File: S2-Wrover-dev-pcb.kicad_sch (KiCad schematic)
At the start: 8 parts, among them P1 CONN_02X13

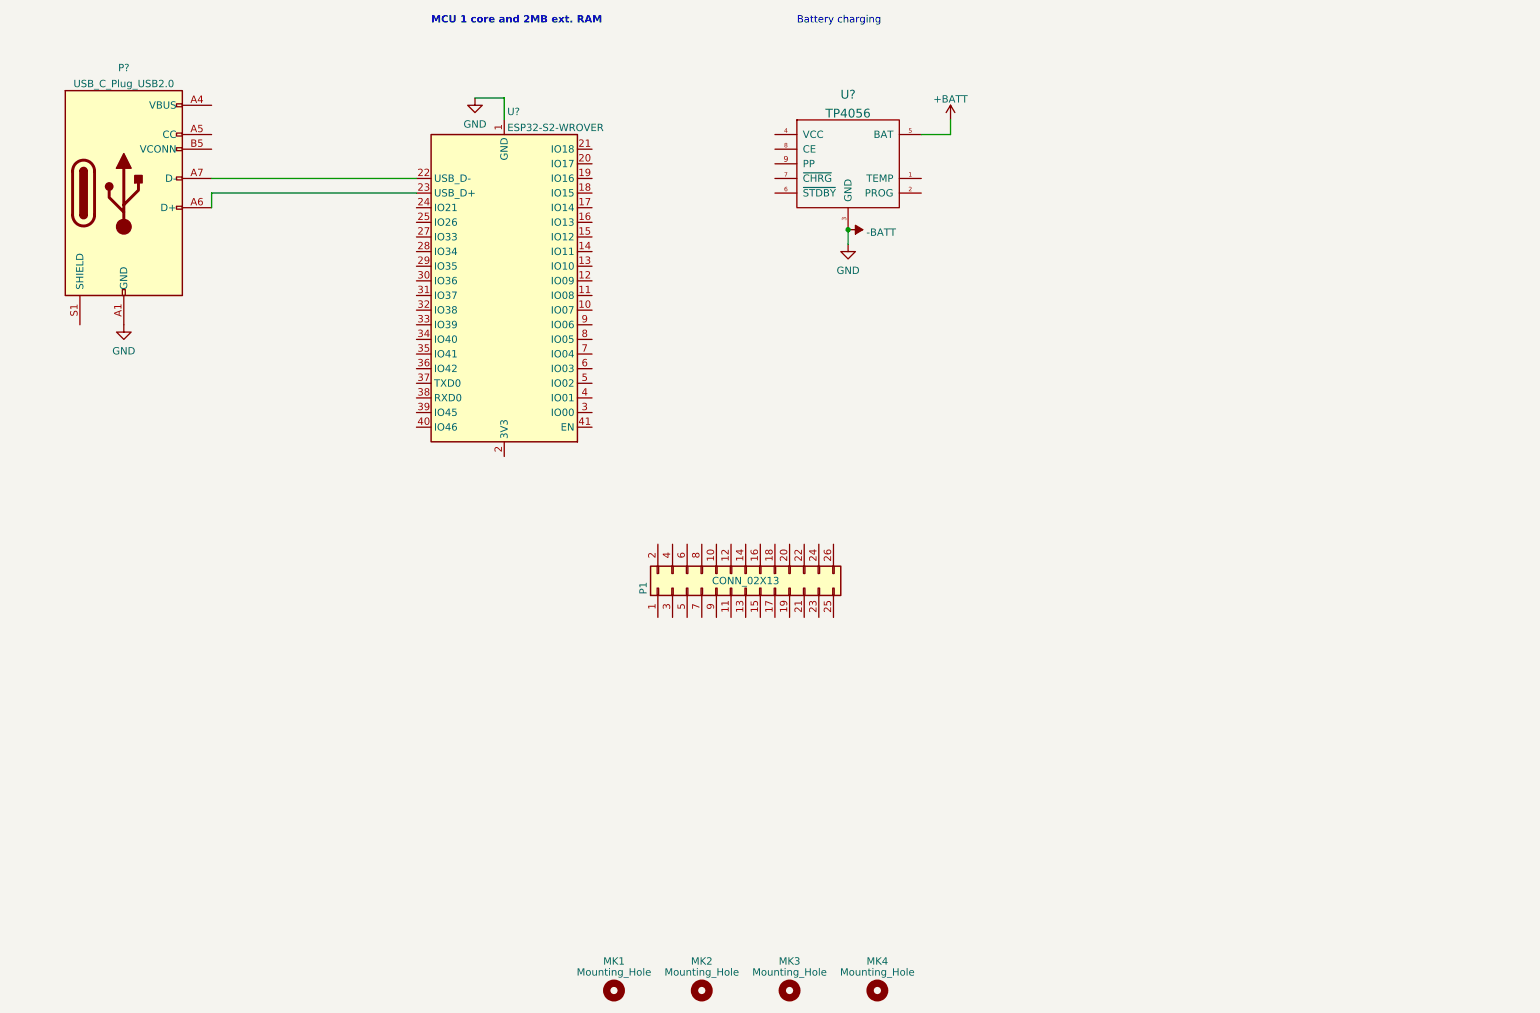
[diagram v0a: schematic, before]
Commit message: Add schematic
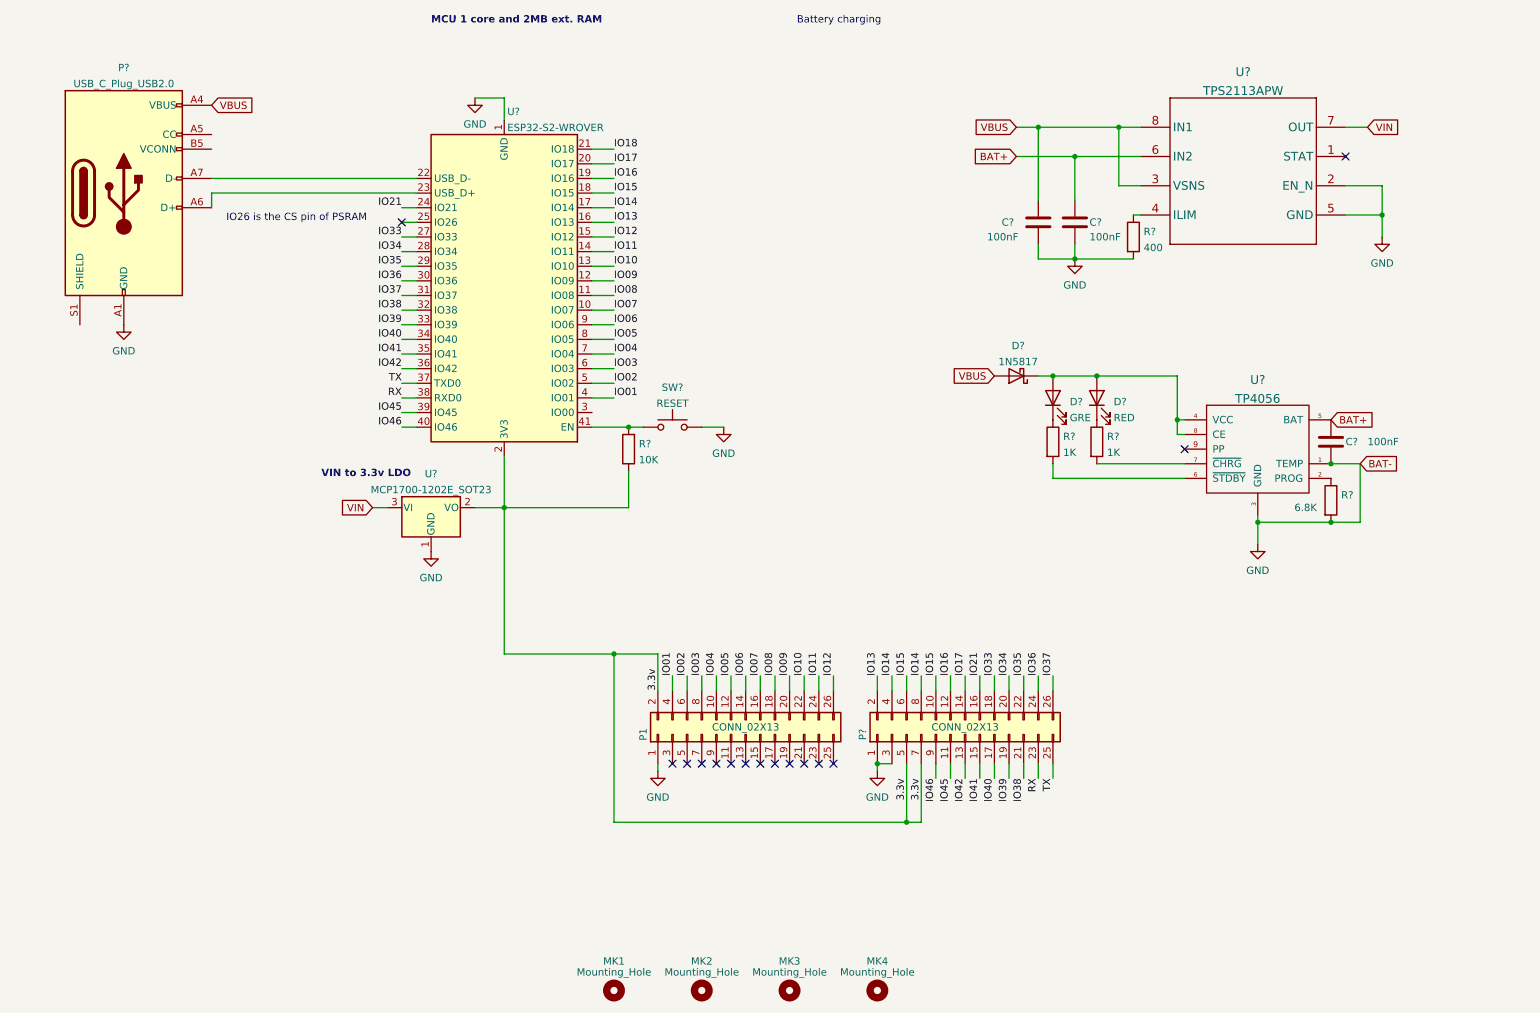
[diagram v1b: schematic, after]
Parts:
- added C? (x3): 100nF, Capacitor_SMD:C_0805_2012Metric, symbol Device:C
- added D?: 1N5817, Diode_SMD:D_SOD-123, symbol Device:D_Schottky
- added D?: RED, LED_SMD:LED_0805_2012Metric, symbol Device:LED
- added D?: GRE, LED_SMD:LED_0805_2012Metric, symbol Device:LED
- added P?: CONN_02X13, Pin_Headers:Pin_Header_Straight_2x13, symbol Connector_Generic:Conn_02x13_Odd_Even
- added R?: 400, Resistor_SMD:R_0603_1608Metric, symbol Device:R
- added R?: 6.8K, Resistor_SMD:R_0603_1608Metric, symbol Device:R
- added R? (x2): 1K, Resistor_SMD:R_0603_1608Metric, symbol Device:R
- added R?: 10K, Resistor_SMD:R_0603_1608Metric, symbol Device:R
- added SW?: RESET, Button_Switch_SMD:SW_SPST_B3U-1000P-B, symbol Switch:SW_Push
- added U?: TPS2113APW, PW0008A_N, symbol epd_breakout:TPS2113APW
- added U?: MCP1700-1202E_SOT23, Package_TO_SOT_SMD:SOT-23, symbol Regulator_Linear:MCP1700-1202E_SOT23
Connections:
- net -BATT is gone; now on net GND: P?.A1 (GND), P?.A12 (GND), P?.B1 (GND), P?.B12 (GND), U?.1 (GND), U?.26 (GND), U?.3 (GND), U?.42 (GND), U?.43 (GND)
- net GND: now reaches P1.1 (Pin_1)
- net GND: now also U?.1 (TEMP), C?.1, C?.1, C?.1, P?.1 (Pin_1), P?.3 (Pin_3), R?.2, R?.2, SW?.2, U?.1 (GND), U?.2 (EN_N), U?.5 (GND)
- net IO04: now reaches P1.10 (Pin_10)
- net IO04: now also U?.7 (IO04)
- net IO05: now reaches P1.12 (Pin_12)
- net IO05: now also U?.8 (IO05)
- net IO06: now reaches P1.14 (Pin_14)
- net IO06: now also U?.9 (IO06)
- net IO07: now reaches P1.16 (Pin_16)
- net IO07: now also U?.10 (IO07)
- net IO08: now reaches P1.18 (Pin_18)
- net IO08: now also U?.11 (IO08)
- net 3.3v: now reaches P1.2 (Pin_2)
- net 3.3v: now also U?.2 (3V3), P?.5 (Pin_5), P?.7 (Pin_7), R?.1, U?.2 (VO)
- net IO09: now reaches P1.20 (Pin_20)
- net IO09: now also U?.12 (IO09)
- net IO10: now reaches P1.22 (Pin_22)
- net IO10: now also U?.13 (IO10)
- net IO11: now reaches P1.24 (Pin_24)
- net IO11: now also U?.14 (IO11)
- net IO12: now reaches P1.26 (Pin_26)
- net IO12: now also U?.15 (IO12)
- net IO01: now reaches P1.4 (Pin_4)
- net IO01: now also U?.4 (IO01)
- net IO02: now reaches P1.6 (Pin_6)
- net IO02: now also U?.5 (IO02)
- net IO03: now reaches P1.8 (Pin_8)
- net IO03: now also U?.6 (IO03)
- net IO13: now reaches U?.16 (IO13)
- net IO13: now also P?.2 (Pin_2)
- net IO14: now reaches U?.17 (IO14)
- net IO14: now also P?.4 (Pin_4), P?.8 (Pin_8)
- net IO15: now reaches U?.18 (IO15)
- net IO15: now also P?.10 (Pin_10), P?.6 (Pin_6)
- net IO16: now reaches U?.19 (IO16)
- net IO16: now also P?.12 (Pin_12)
- net IO17: now reaches U?.20 (IO17)
- net IO17: now also P?.14 (Pin_14)
- net IO18: now reaches U?.21 (IO18)
- net IO21: now reaches U?.24 (IO21)
- net IO21: now also P?.16 (Pin_16)
- net IO33: now reaches U?.27 (IO33)
- net IO33: now also P?.18 (Pin_18)
- net IO34: now reaches U?.28 (IO34)
- net IO34: now also P?.20 (Pin_20)
- net IO35: now reaches U?.29 (IO35)
- net IO35: now also P?.22 (Pin_22)
- net IO36: now reaches U?.30 (IO36)
- net IO36: now also P?.24 (Pin_24)
- net IO37: now reaches U?.31 (IO37)
- net IO37: now also P?.26 (Pin_26)
- net IO38: now reaches U?.32 (IO38)
- net IO38: now also P?.21 (Pin_21)
- net IO39: now reaches U?.33 (IO39)
- net IO39: now also P?.19 (Pin_19)
- net IO40: now reaches U?.34 (IO40)
- net IO40: now also P?.17 (Pin_17)
- net IO41: now reaches U?.35 (IO41)
- net IO41: now also P?.15 (Pin_15)
- net IO42: now reaches U?.36 (IO42)
- net IO42: now also P?.13 (Pin_13)
- net TX: now reaches U?.37 (TXD0)
- net TX: now also P?.25 (Pin_25)
- net RX: now reaches U?.38 (RXD0)
- net RX: now also P?.23 (Pin_23)
- net IO45: now reaches U?.39 (IO45)
- net IO45: now also P?.11 (Pin_11)
- net IO46: now reaches U?.40 (IO46)
- net IO46: now also P?.9 (Pin_9)
- net at U?.41 (EN): now also R?.2, SW?.1
- net VBUS: now reaches P?.A4 (VBUS), P?.A9 (VBUS), P?.B4 (VBUS), P?.B9 (VBUS)
- net VBUS: now also C?.2, D?.2 (A), U?.3 (VSNS), U?.8 (IN1)
- net at U?.2 (PROG): now also R?.1
- net at U?.4 (VCC): now also U?.8 (CE), D?.1 (K), D?.2 (A), D?.2 (A)
- net at U?.6 (~{STDBY}): now also R?.2
- net at U?.7 (~{CHRG}): now also R?.2
- net +BATT renamed BAT+
- net BAT+: now also C?.2, C?.2, U?.6 (IN2)
- new net: D?.1 (K), R?.1 (x2)
- new net: R?.1, U?.4 (ILIM)
- new net VIN: U?.3 (VI), U?.7 (OUT)
- no-connect marks 0 -> 15
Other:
- note added: "IO26 is the CS pin of PSRAM"
- note added: "VIN to 3.3v LDO"
- moved on the sheet: P1, U?

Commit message: Add BOOT switch
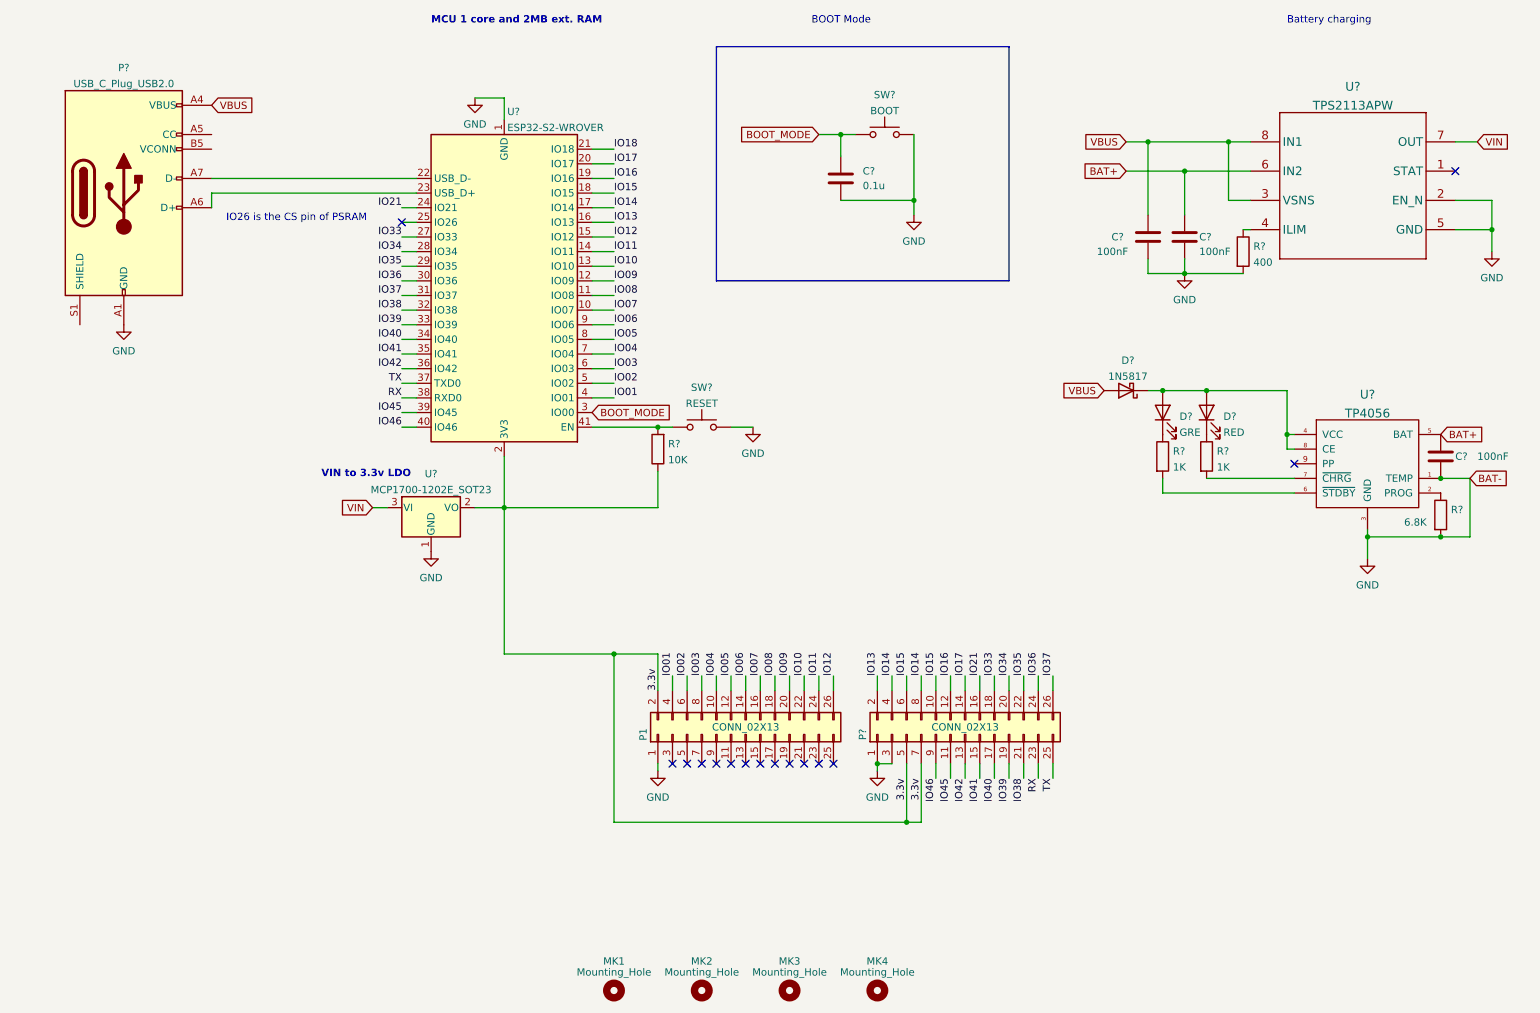
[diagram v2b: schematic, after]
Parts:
- added C?: 0.1u, Capacitor_SMD:C_0805_2012Metric, symbol Device:C
- added SW?: BOOT, footprint:Alps_SKRK, symbol Switch:SW_Push
- SW?: footprint Button_Switch_SMD:SW_SPST_B3U-1000P-B -> footprint:Alps_SKRK
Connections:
- net GND: now also C?.1, SW?.2
- net BOOT_MODE: now reaches U?.3 (IO00)
- net BOOT_MODE: now also C?.2, SW?.1
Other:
- note added: "BOOT Mode"
- moved on the sheet: C?, D?, R?, SW?, U?

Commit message: ERC needs to pass
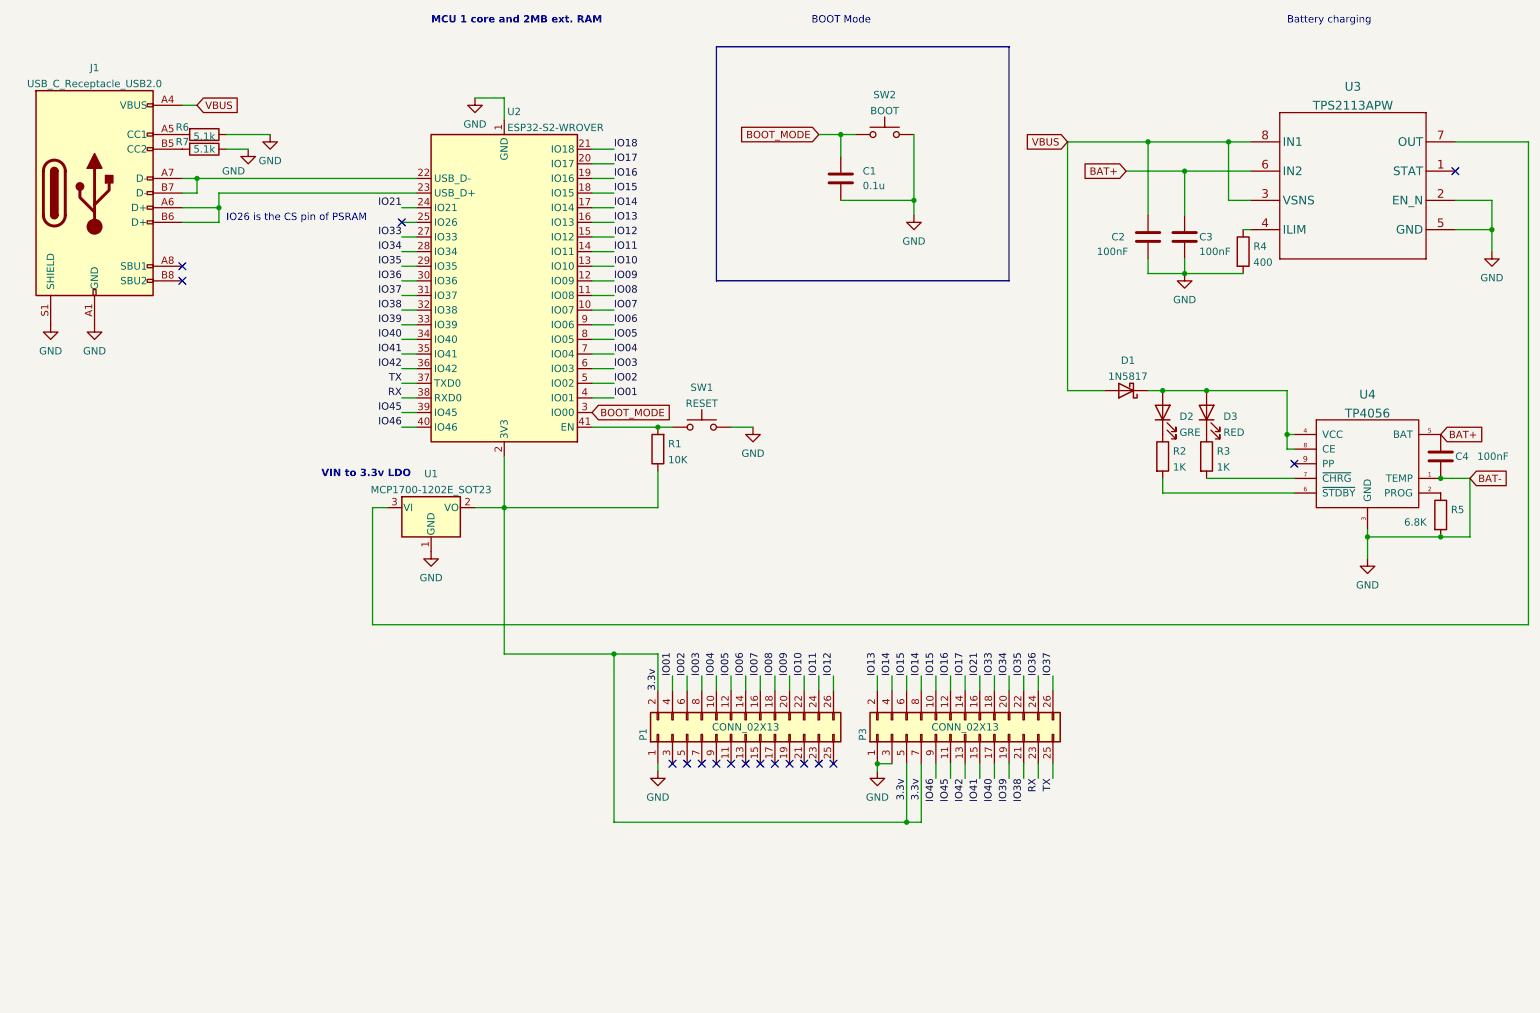
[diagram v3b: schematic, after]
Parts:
- removed MK1, MK2, MK3, MK4: Mounting_Hole, Mounting_Holes:MountingHole_3-5mm, symbol minnowboard-ls-lure:Mounting_Hole-Mechanical
- removed P?: USB_C_Plug_USB2.0, symbol Connector:USB_C_Plug_USB2.0
- added J1: USB_C_Receptacle_USB2.0, footprint:USB_C_Receptacle_HRO_TYPE-C-31-M-12, symbol Connector:USB_C_Receptacle_USB2.0
- added R6, R7: 5.1k, Resistor_SMD:R_0603_1608Metric, symbol Device:R
- gave numbers to parts that had none: 19
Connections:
- net GND: now also J1.A1 (GND), J1.A12 (GND), J1.B1 (GND), J1.B12 (GND), J1.S1 (SHIELD), R6.1, R7.1
- net VBUS: now also J1.A4 (VBUS), J1.A9 (VBUS), J1.B4 (VBUS), J1.B9 (VBUS)
- net at U2.22 (USB_D-): now also J1.A7 (D-), J1.B7 (D-)
- net at U2.23 (USB_D+): now also J1.A6 (D+), J1.B6 (D+)
- net VIN: no longer names the net of U1.3 (VI), U3.7 (OUT)
- new net: J1.A5 (CC1), R6.2
- new net: J1.B5 (CC2), R7.2
- no-connect marks 15 -> 17
